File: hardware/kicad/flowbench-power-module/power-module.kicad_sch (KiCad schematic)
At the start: 29 parts, among them J1 Power header, J2 Signal header, Q1 N-ch >=80 V, Rds(on) <=15 mOh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, Q2 BSS138, U1 TPS26631PWP, U2 TPS7A4901DGN

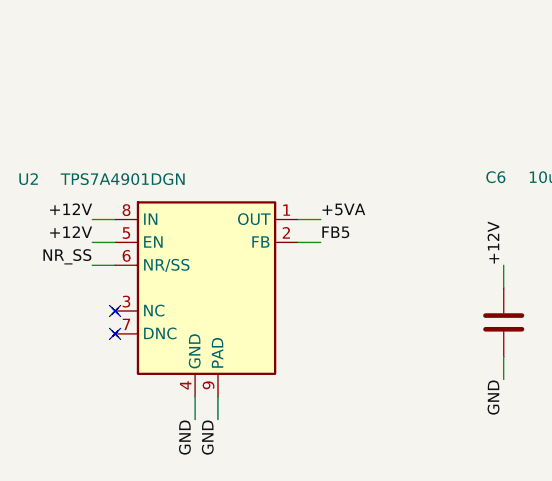
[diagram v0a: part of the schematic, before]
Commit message: KiCad: fix off-grid pins on ADS1219 and AM26C31 symbols
A floating-point modulo misread the symbol half-height as off-grid and
shifted it by half a step, leaving top and bottom pins 0.635 mm off the
1.27 mm connection grid (16 ERC warnings). verify.py now checks every pin
and wire end against the grid.

Co-Authored-By: Claude Opus 5.5 <noreply@anthropic.com>
Claude-Session: https://claude.ai/code/session_01QEmmugJA9S77dSDSNcKrPa
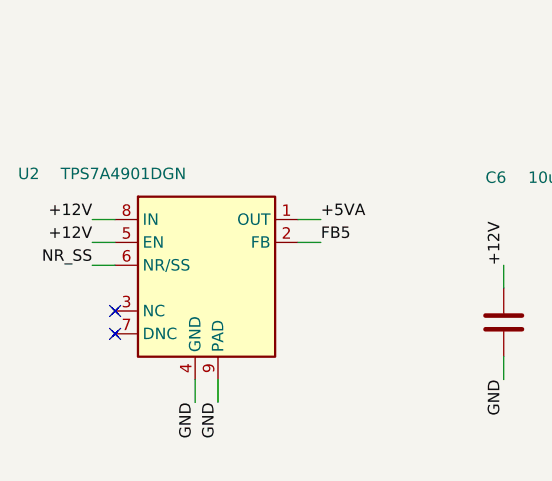
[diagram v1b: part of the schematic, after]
